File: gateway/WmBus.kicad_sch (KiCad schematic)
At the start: 24 parts, among them IC1201 MIC5317-3.3xM5, IC1202 74LVC1G07, IC1203 TXB0102DCT, M1201 iM891A-XL

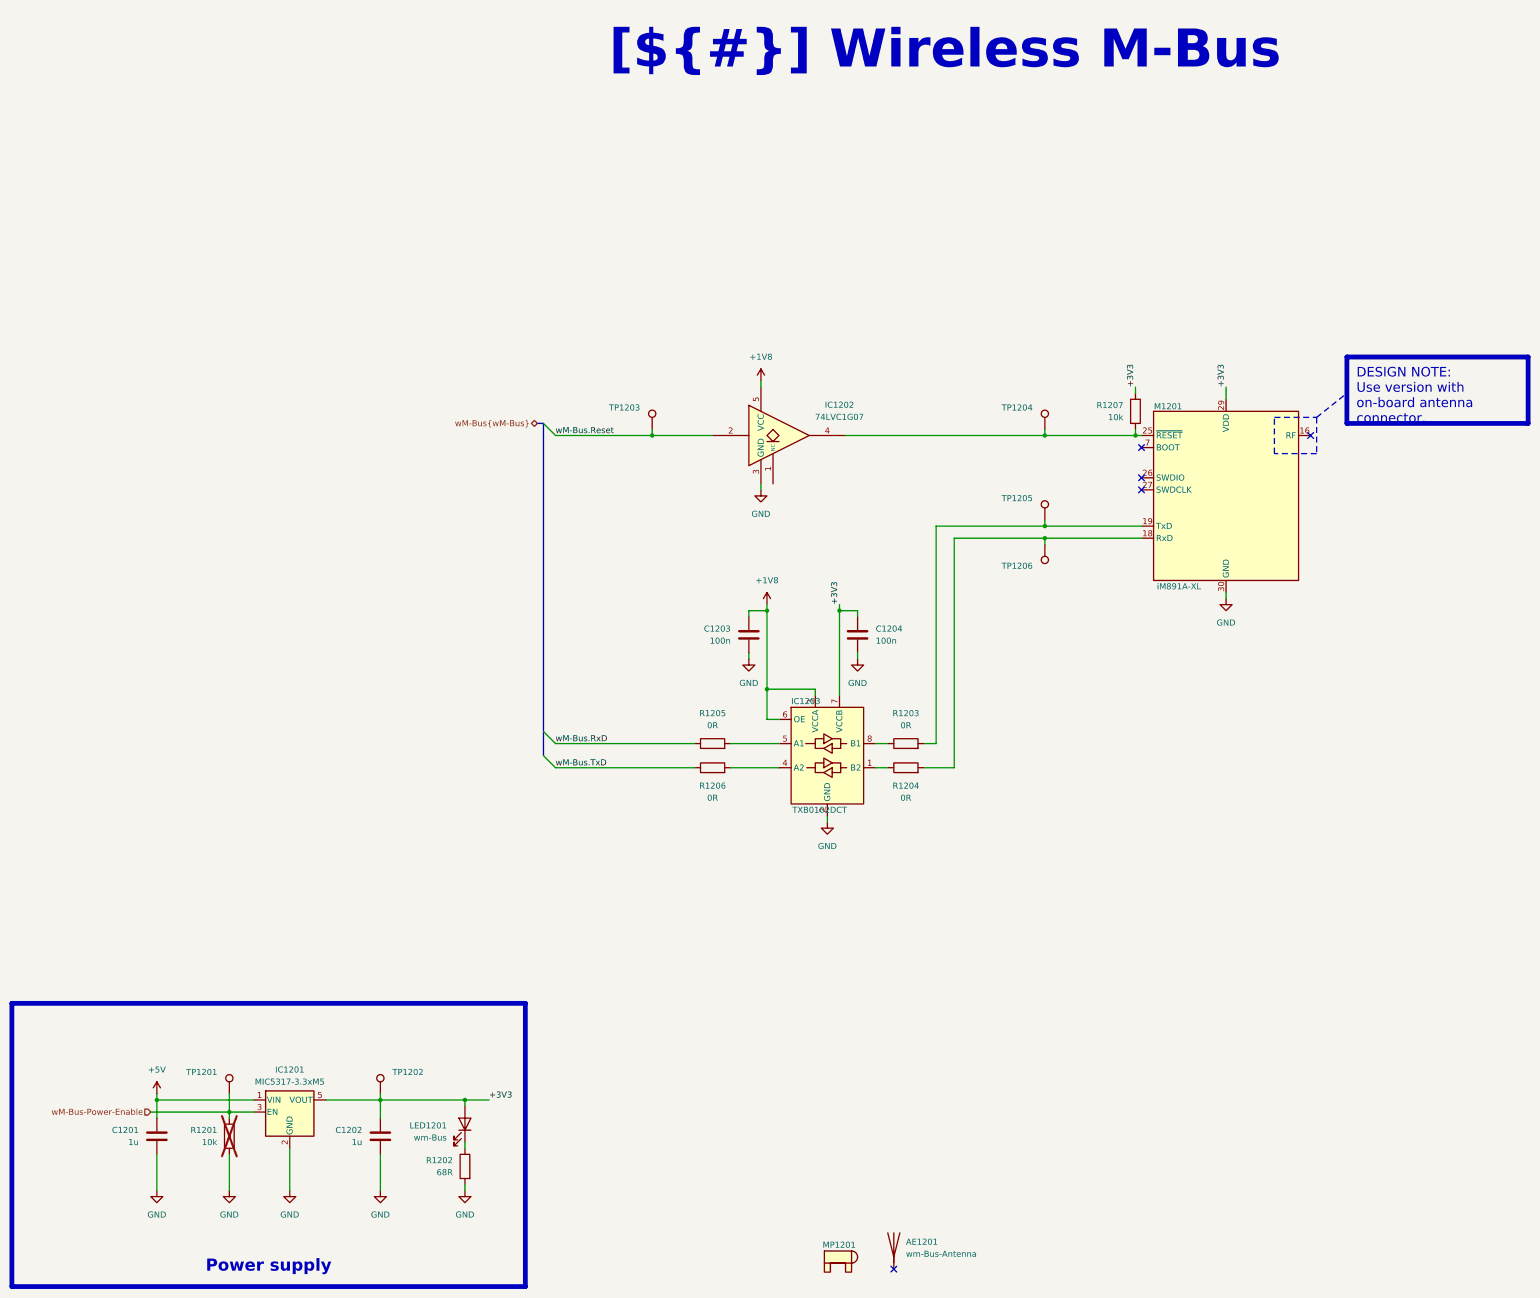
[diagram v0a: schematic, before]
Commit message: Add INA219 for current measurement
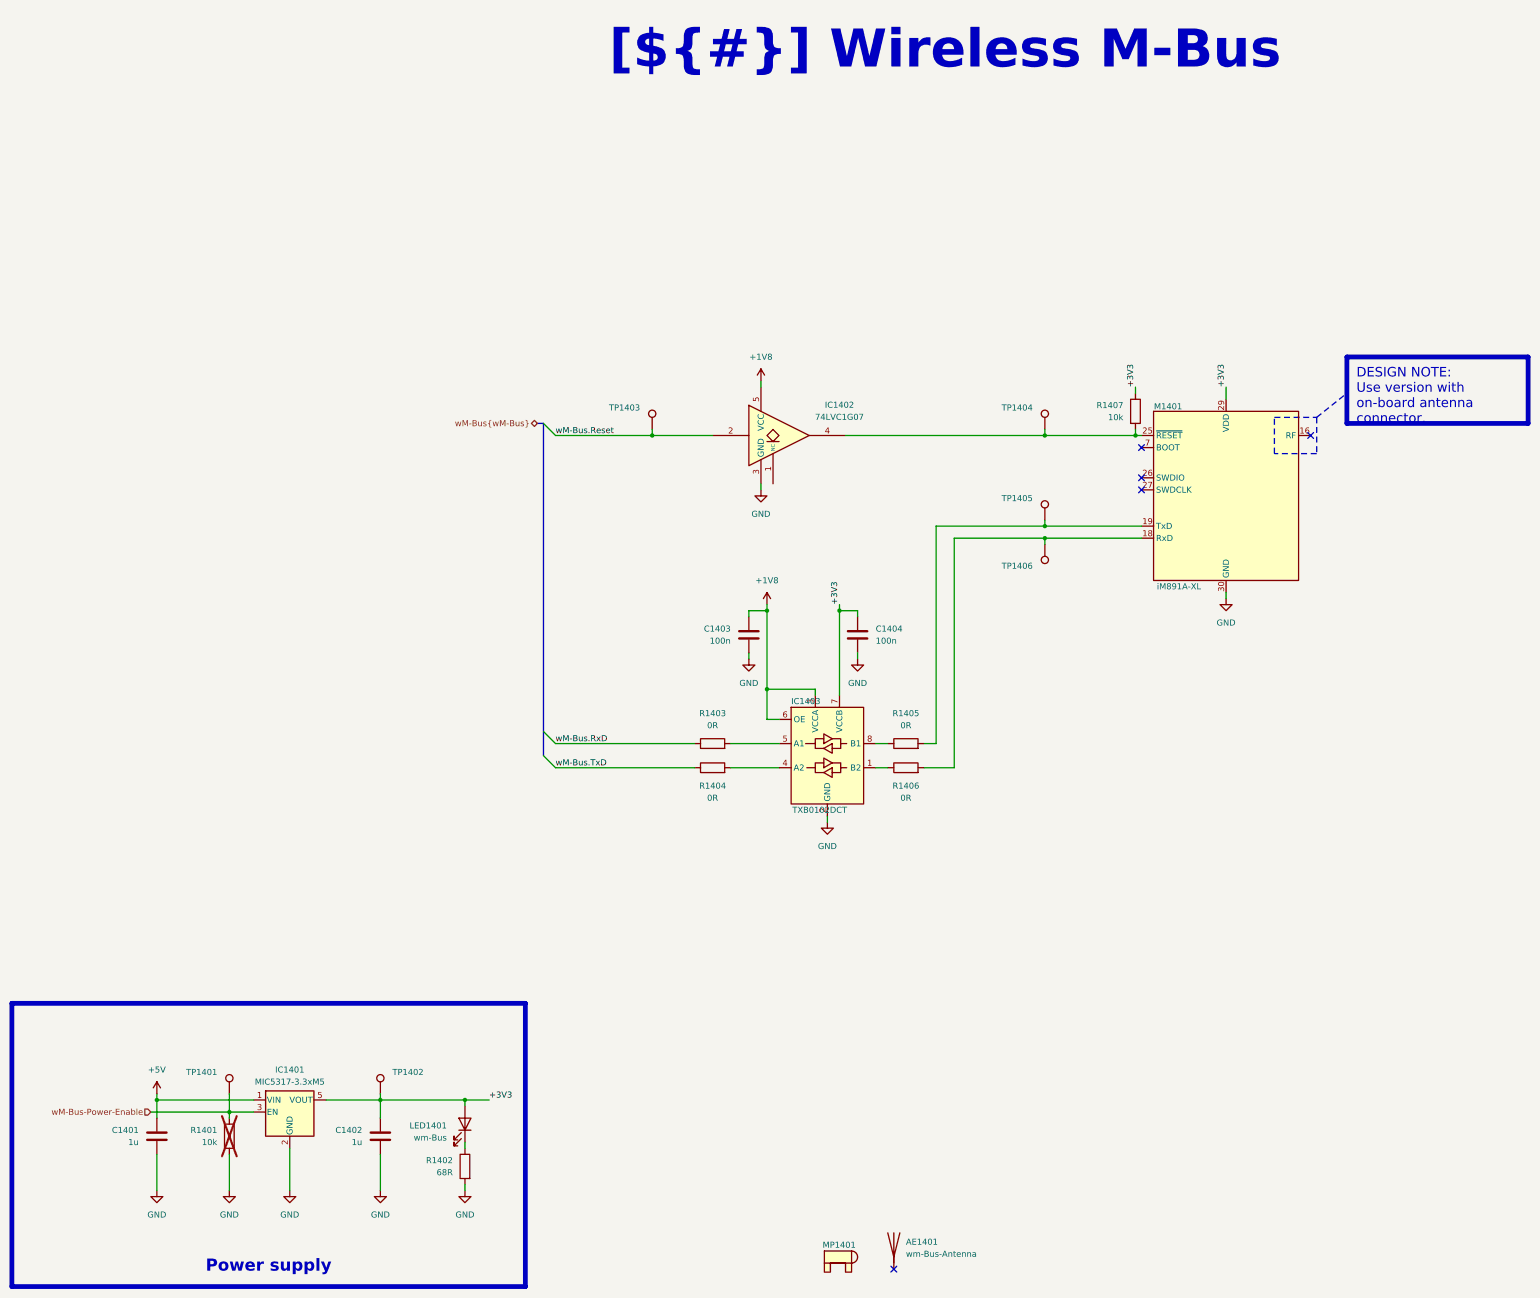
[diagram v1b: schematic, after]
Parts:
- renumbered AE1201 to AE1401, C1201 to C1401, C1202 to C1402, C1203 to C1403, C1204 to C1404, IC1201 to IC1401, IC1202 to IC1402, IC1203 to IC1403, LED1201 to LED1401, M1201 to M1401, MP1201 to MP1401, R1201 to R1401, R1202 to R1402, R1205 to R1403, R1206 to R1404, R1203 to R1405, R1204 to R1406, R1207 to R1407, TP1201 to TP1401, TP1202 to TP1402, TP1203 to TP1403, TP1204 to TP1404, TP1205 to TP1405, TP1206 to TP1406

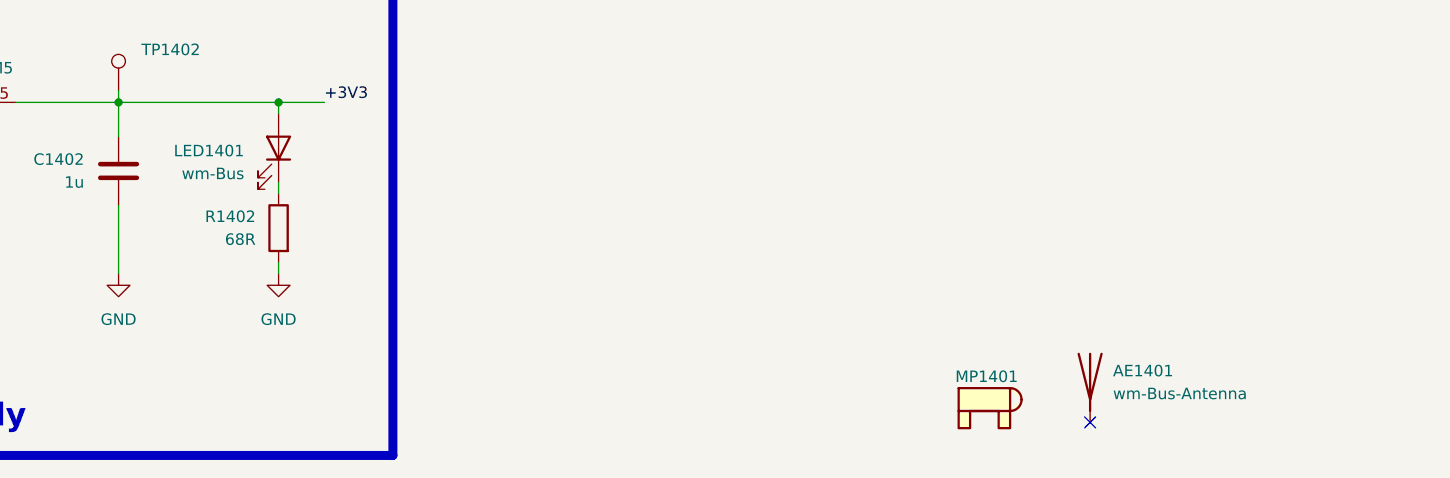
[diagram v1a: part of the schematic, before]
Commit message: Improving Thread
- Add boot signal for Thread MCU
- Add debug LED for nRF5340
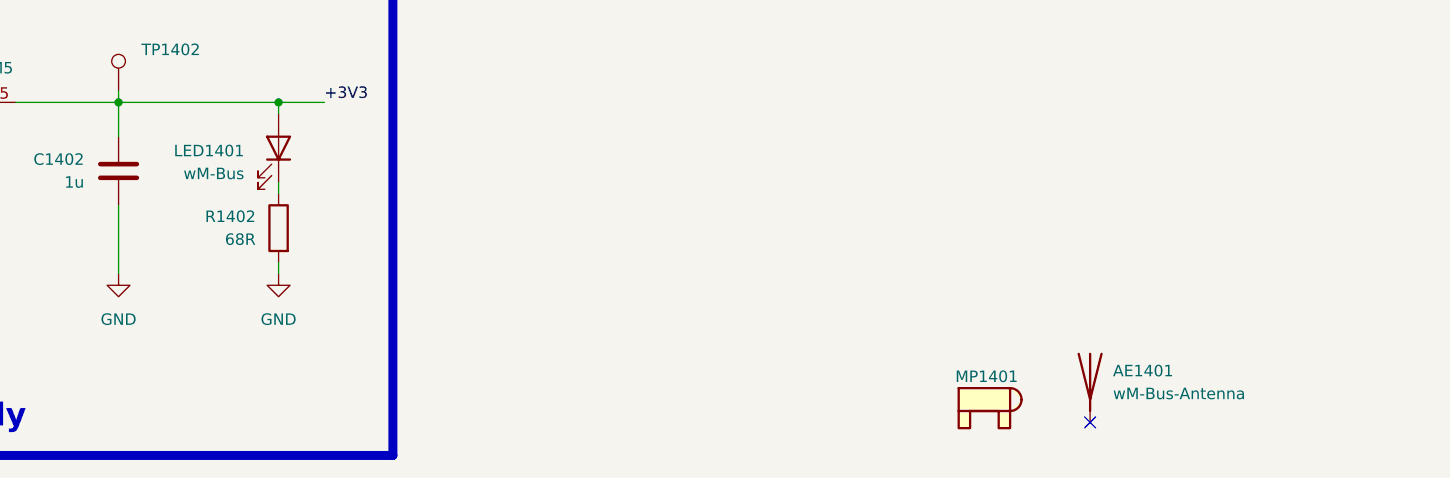
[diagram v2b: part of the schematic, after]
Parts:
- AE1401: value wm-Bus-Antenna -> wM-Bus-Antenna
- LED1401: value wm-Bus -> wM-Bus
- TP1401, TP1402, TP1403, TP1404, TP1405, TP1406: value ~ -> (none)
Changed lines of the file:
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@@
 			)
 		)
-		(property "Value" "~"
+		(property "Value" ""
 			(at 228.6 129.0321 0)
 			(show_name no)
@@
 			)
 		)
-		(property "Value" "~"
+		(property "Value" ""
 			(at 57.15 240.5379 0)
 			(show_name no)
@@
 			)
 		)
-		(property "Value" "~"
+		(property "Value" ""
 			(at 93.98 240.5379 0)
 			(show_name no)
@@
 			)
 		)
-		(property "Value" "wm-Bus"
+		(property "Value" "wM-Bus"
 			(at 105.41 251.7774 90)
 			(show_name no)
@@
 			)
 		)
-		(property "Value" "~"
+		(property "Value" ""
 			(at 146.05 100.8379 0)
 			(show_name no)
@@
 			)
 		)
-		(property "Value" "~"
+		(property "Value" ""
 			(at 228.6 100.8379 0)
 			(show_name no)
@@
 			)
 		)
-		(property "Value" "~"
+		(property "Value" ""
 			(at 228.6 119.8879 0)
 			(show_name no)
@@
 			)
 		)
-		(property "Value" "wm-Bus-Antenna"
+		(property "Value" "wM-Bus-Antenna"
 			(at 201.93 276.2249 0)
 			(show_name no)
